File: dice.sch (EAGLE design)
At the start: 10 parts

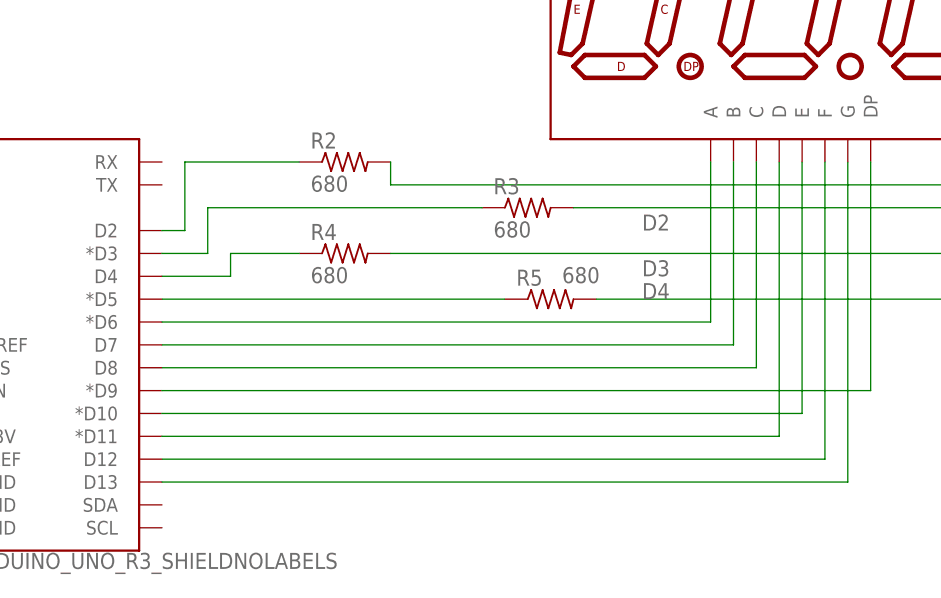
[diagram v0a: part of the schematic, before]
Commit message: Connect all traces except GND
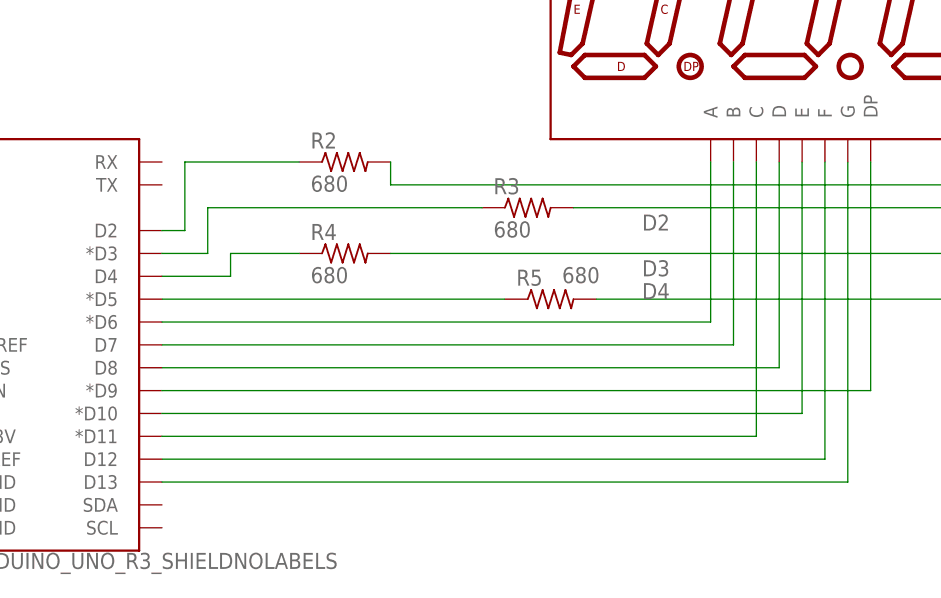
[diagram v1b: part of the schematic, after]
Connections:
- net N$1 renamed LED
- net C: now also B1.*D11; no longer B1.D8
- net D: now also B1.D8, DISP1.D; no longer B1.D13, DISP1.G
- net F: now also B1.D12, DISP1.F; no longer B1.*D11, DISP1.D
- net G: now also B1.D13, DISP1.G; no longer B1.D12, DISP1.F
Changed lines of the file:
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@@
 </segment>
 </net>
-<net name="N$1" class="0">
+<net name="LED" class="0">
 <segment>
 <pinref part="B1" gate="G$1" pin="A4"/>
@@
 </segment>
 </net>
-<net name="C" class="0">
+<net name="D" class="0">
 <segment>
 <pinref part="B1" gate="G$1" pin="D8"/>
-<pinref part="DISP1" gate="G$1" pin="C"/>
-<wire x1="83.82" y1="50.8" x2="149.86" y2="50.8" width="0.1524" layer="91"/>
-<wire x1="149.86" y1="50.8" x2="149.86" y2="73.66" width="0.1524" layer="91"/>
+<wire x1="83.82" y1="50.8" x2="152.4" y2="50.8" width="0.1524" layer="91"/>
+<pinref part="DISP1" gate="G$1" pin="D"/>
+<wire x1="152.4" y1="50.8" x2="152.4" y2="73.66" width="0.1524" layer="91"/>
 </segment>
 </net>
@@
 </segment>
 </net>
-<net name="F" class="0">
+<net name="C" class="0">
 <segment>
 <pinref part="B1" gate="G$1" pin="*D11"/>
-<wire x1="83.82" y1="43.18" x2="152.4" y2="43.18" width="0.1524" layer="91"/>
-<pinref part="DISP1" gate="G$1" pin="D"/>
-<wire x1="152.4" y1="73.66" x2="152.4" y2="43.18" width="0.1524" layer="91"/>
+<wire x1="83.82" y1="43.18" x2="149.86" y2="43.18" width="0.1524" layer="91"/>
+<pinref part="DISP1" gate="G$1" pin="C"/>
+<wire x1="149.86" y1="73.66" x2="149.86" y2="43.18" width="0.1524" layer="91"/>
 </segment>
 </net>
-<net name="G" class="0">
+<net name="F" class="0">
 <segment>
 <pinref part="B1" gate="G$1" pin="D12"/>
@@
 </segment>
 </net>
-<net name="D" class="0">
+<net name="G" class="0">
 <segment>
 <pinref part="B1" gate="G$1" pin="D13"/>

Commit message: Add GND pours
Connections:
- net GND: no longer B1.GND@0, B1.GND@1
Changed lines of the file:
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@@
 <junction x="40.64" y="38.1"/>
 <pinref part="D1" gate="D1" pin="C"/>
-<wire x1="55.88" y1="38.1" x2="55.88" y2="35.56" width="0.1524" layer="91"/>
 <junction x="55.88" y="38.1"/>
-<pinref part="B1" gate="G$1" pin="GND@1"/>
-<wire x1="55.88" y1="35.56" x2="58.42" y2="35.56" width="0.1524" layer="91"/>
-<wire x1="55.88" y1="35.56" x2="55.88" y2="33.02" width="0.1524" layer="91"/>
-<junction x="55.88" y="35.56"/>
-<pinref part="B1" gate="G$1" pin="GND@0"/>
-<wire x1="55.88" y1="33.02" x2="58.42" y2="33.02" width="0.1524" layer="91"/>
 <pinref part="V1" gate="G$1" pin="2"/>
 <wire x1="45.72" y1="15.24" x2="55.88" y2="15.24" width="0.1524" layer="91"/>
-<wire x1="55.88" y1="15.24" x2="55.88" y2="33.02" width="0.1524" layer="91"/>
-<junction x="55.88" y="33.02"/>
+<wire x1="55.88" y1="15.24" x2="55.88" y2="38.1" width="0.1524" layer="91"/>
 <label x="50.8" y="12.7" size="1.778" layer="95"/>
 </segment>

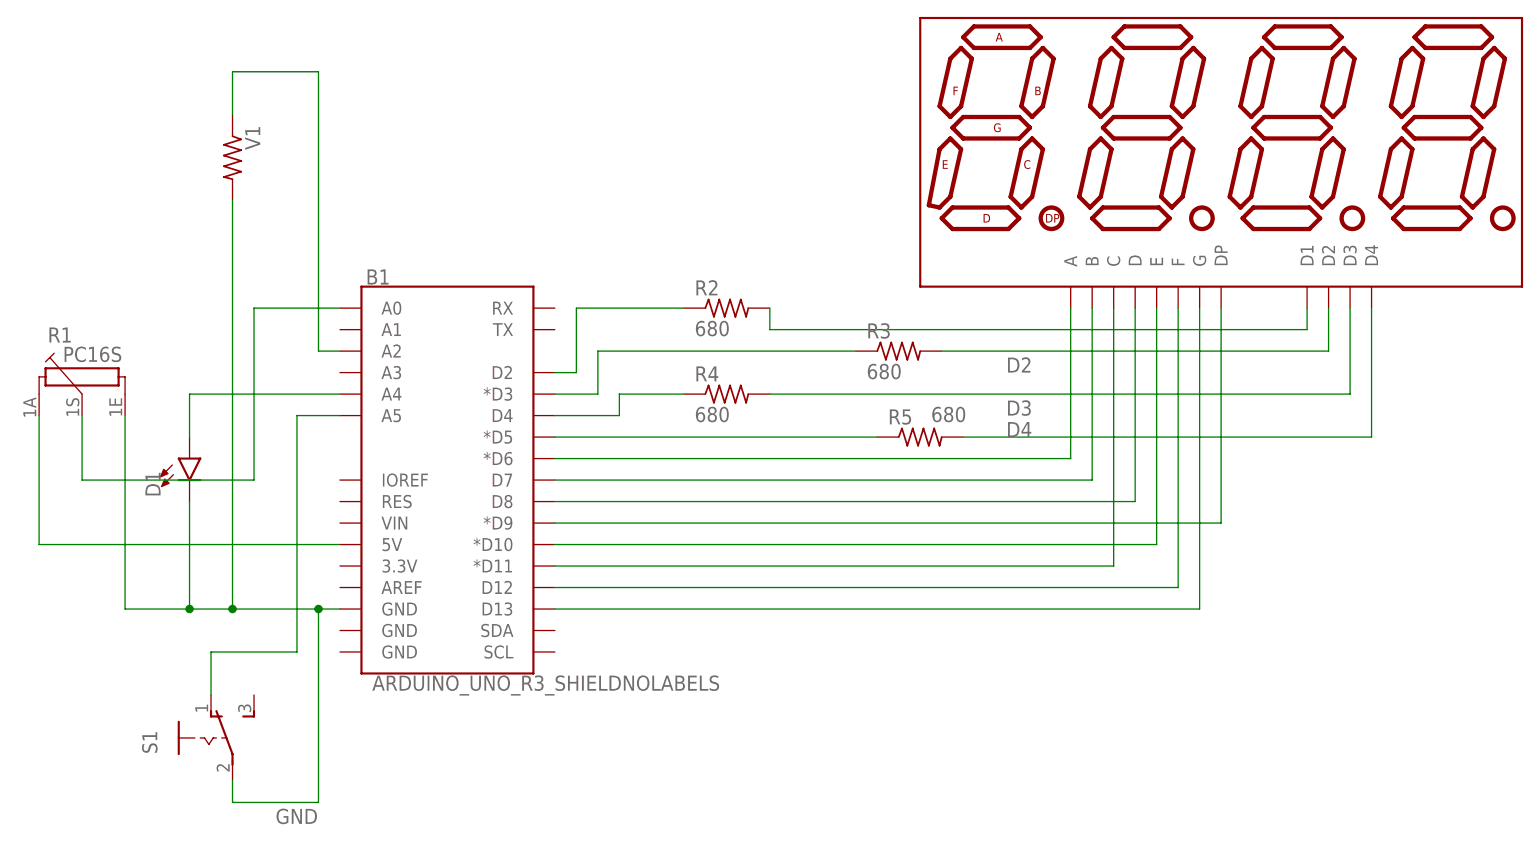
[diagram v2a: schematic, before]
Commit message: Redo PCB for milling
Switch to one layer

Remove ground pours

Switch to 30mil trace width

Add circles of trace around every pad

Reduce hole size on shield and 7 segment display
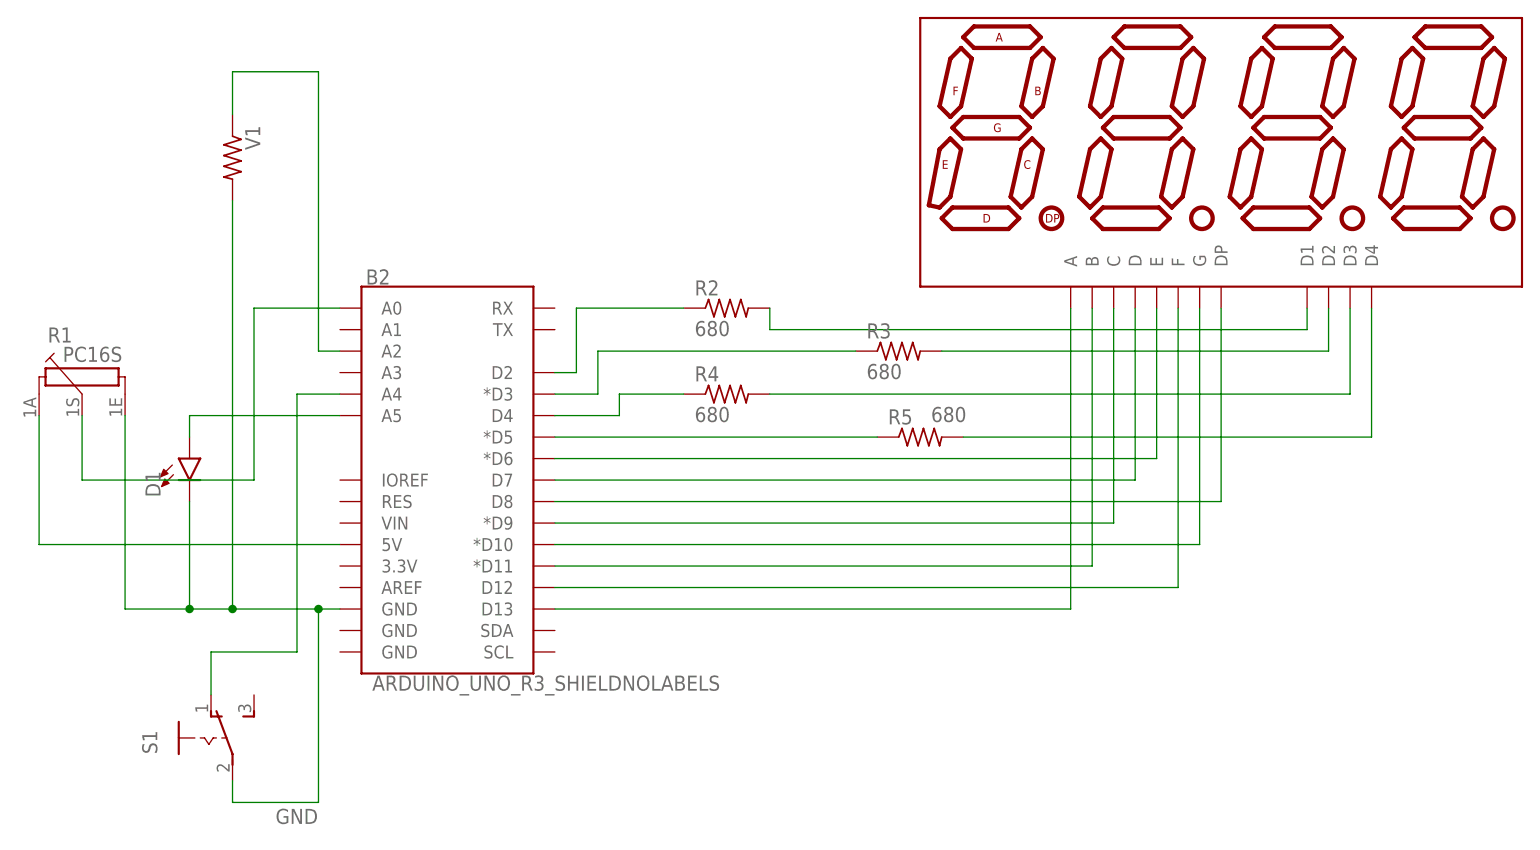
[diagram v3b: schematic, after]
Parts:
- removed B1: ARDUINO_UNO_R3_SHIELDNOLABELS, SparkFun-Boards:ARDUINO_UNO_R3_SHIELDNOLABELS
- added B2: ARDUINO_UNO_R3_SHIELDNOLABELS, SparkFun-Boards-mtr:ARDUINO_UNO_R3_SHIELDNOLABELS
- DISP1: device SparkFun-LED:7-SEGMENT-4DIGIT-20MM-BLUE -> SparkFun-LED-mtr:7-SEGMENT-4DIGIT-20MM-BLUE
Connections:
- net A: now also B2.D13; no longer B1.*D6
- net B: now also B2.*D11; no longer B1.D7
- net C: now also B2.*D9; no longer B1.*D11
- net D: now also B2.D7; no longer B1.D8
- net D1G: now also B2.D2; no longer B1.D2
- net D2G: now also B2.*D3; no longer B1.*D3
- net D3G: now also B2.D4; no longer B1.D4
- net D4G: now also B2.*D5; no longer B1.*D5
- net DP: now also B2.D8; no longer B1.*D9
- net E: now also B2.*D6; no longer B1.*D10
- net F: now also B2.D12; no longer B1.D12
- net G: now also B2.*D10; no longer B1.D13
- net GND: now also B2.GND@2; no longer B1.GND@2
- net LED: now also B2.A5; no longer B1.A4
- net POT: now also B2.A0; no longer B1.A0
- net SW: now also B2.A4; no longer B1.A5
- net VCC: now also B2.5V; no longer B1.5V
- net VIBR: now also B2.A2; no longer B1.A2
